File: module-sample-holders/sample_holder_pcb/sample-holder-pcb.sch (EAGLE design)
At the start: 12 parts, among them IC1 25AA040ST, IC2 DSPIC33CK256MP502-I_SS, Q1 PSMN013-30MLC, Q2 PSMN013-30MLC

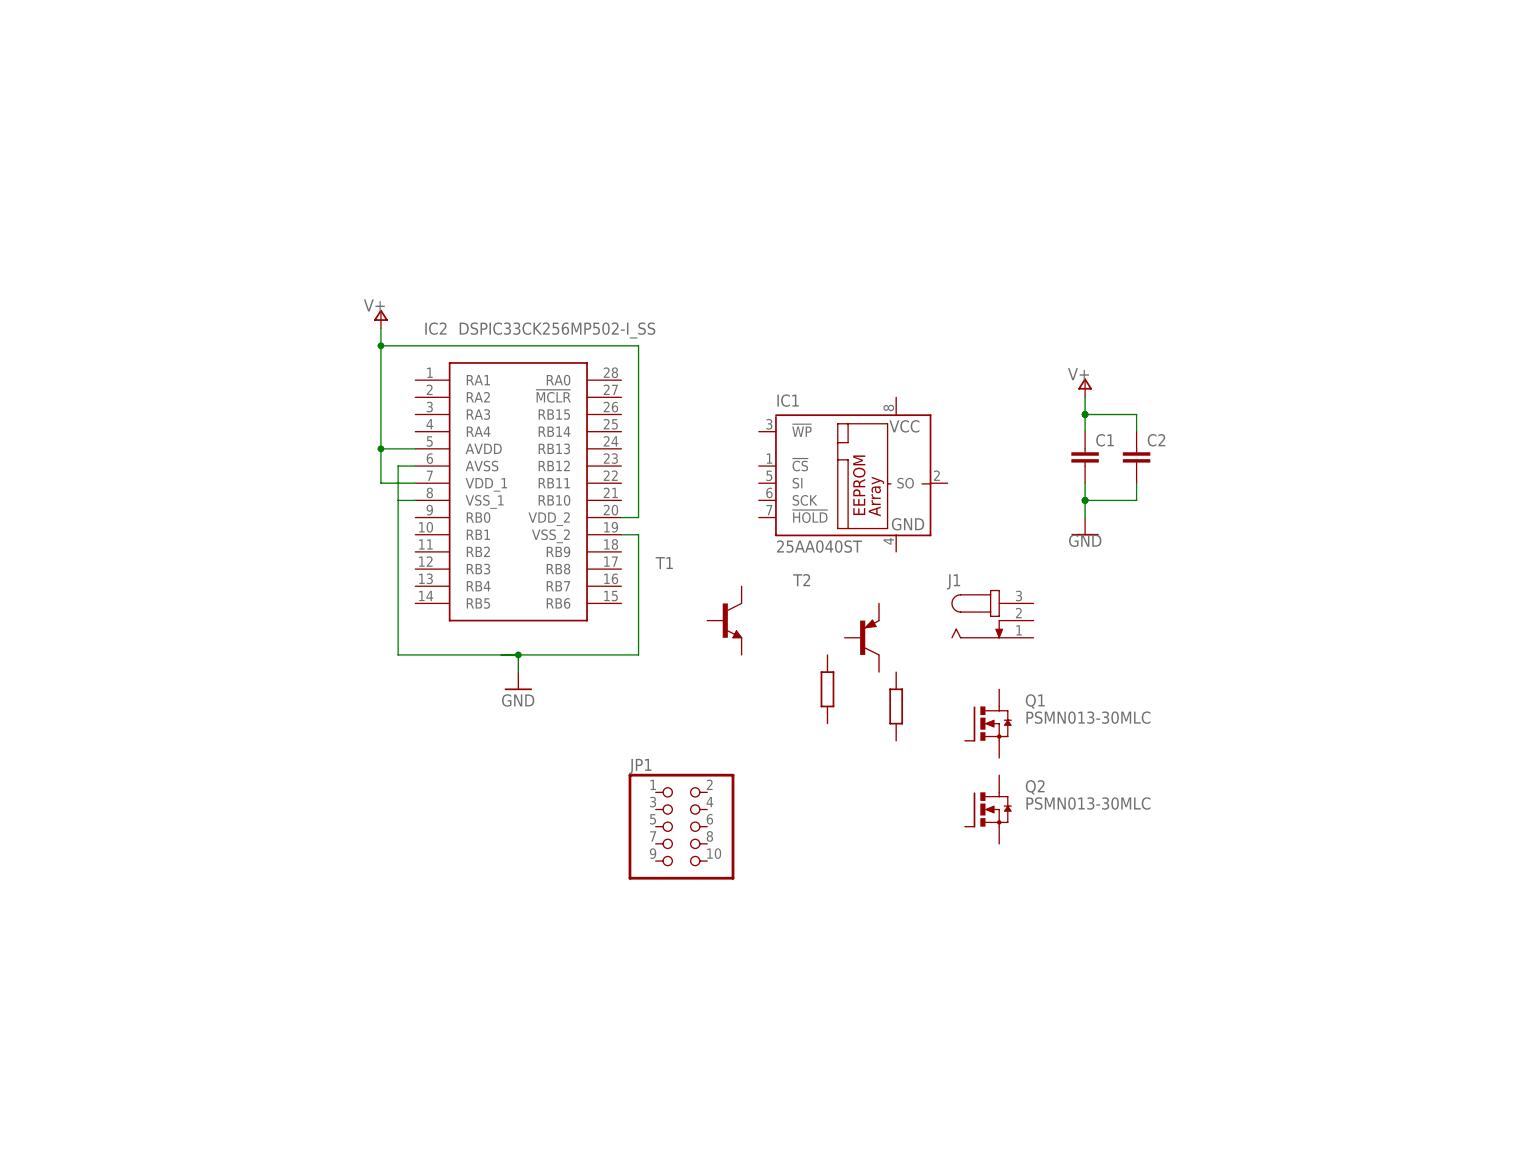
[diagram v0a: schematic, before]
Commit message: Submitting old PCB design before replacing with new design.
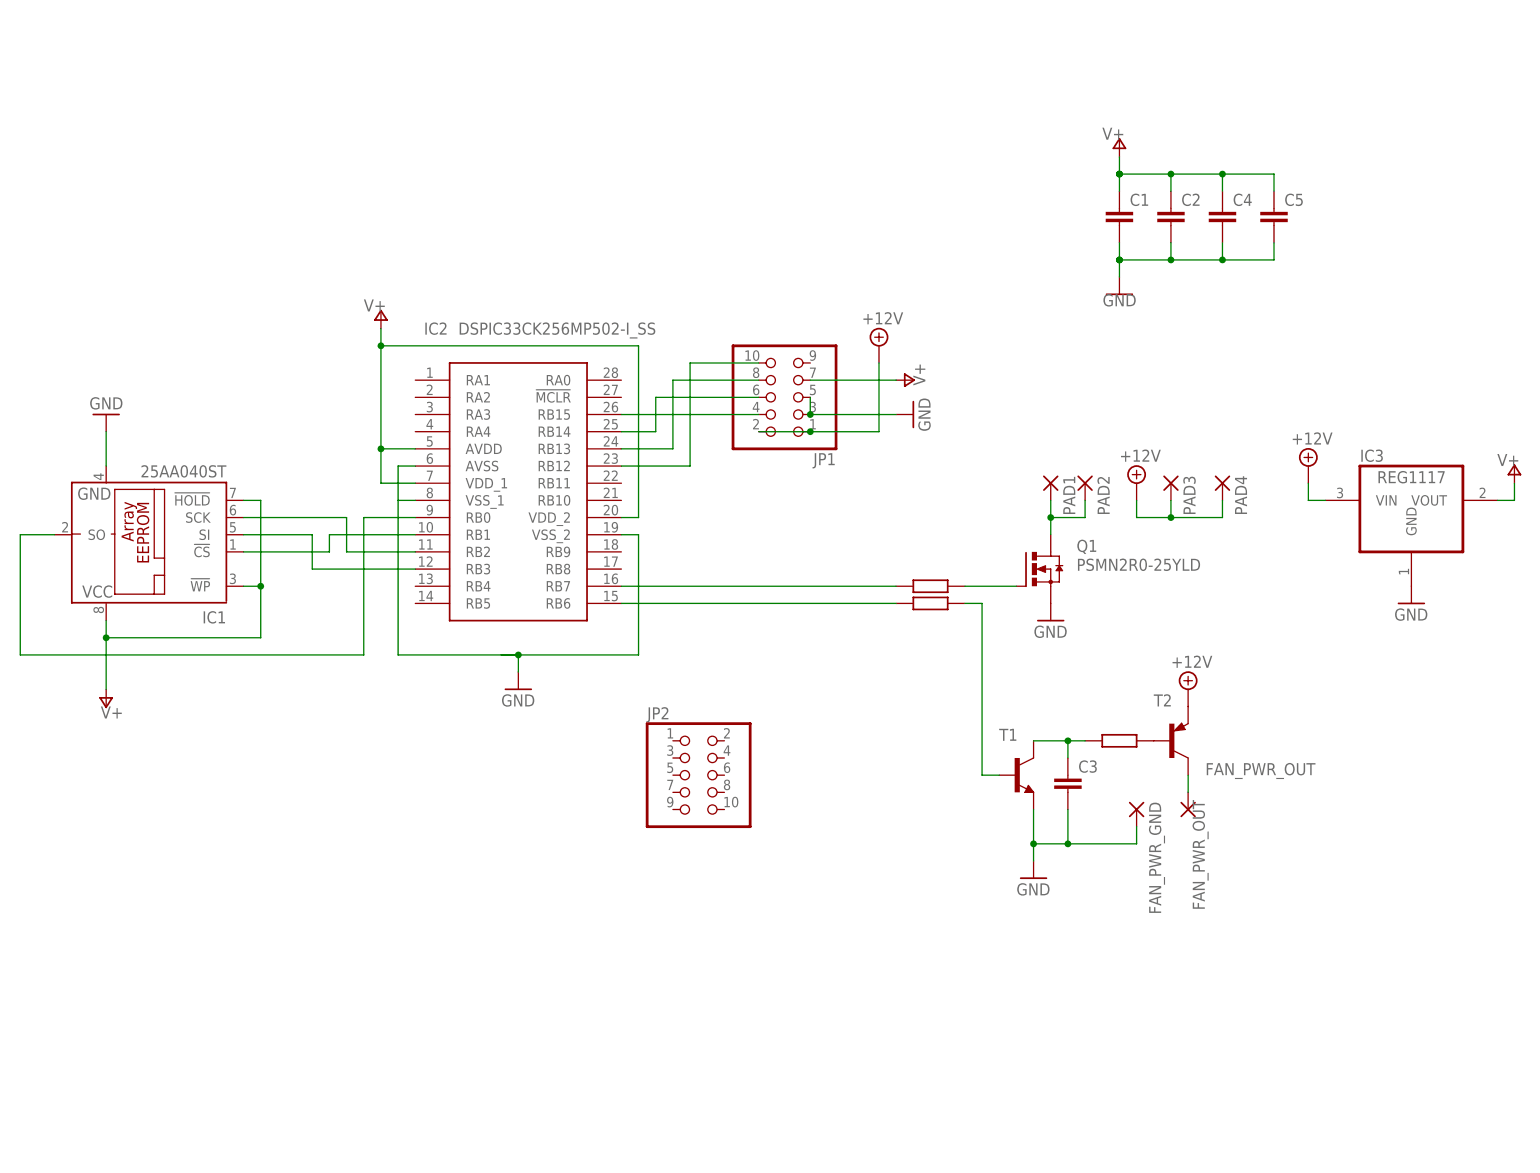
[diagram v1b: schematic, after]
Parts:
- removed J1: (no value), con-jack:JACK-PLUG1
- removed Q2: PSMN013-30MLC, transistor-power:PSMN013-30MLC
- added C3, C4, C5: (no value), rcl:C-EUC1206
- added FAN_PWR_GND, FAN_PWR_OUT: (no value), wirepad:1,6/0,8
- added IC3: REG1117, burr-brown:REG1117
- added JP2: (no value), pinhead:PINHD-2X5/90
- added PAD1, PAD2, PAD3, PAD4: (no value), wirepad:2,54/1,0
- added R3: (no value), rcl:R-EU_R1206
- Q1: MPN (none) -> PSMN2R0-25YLD
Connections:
- new net +12V: IC3.VIN, JP1.1, JP1.2, PAD3.P, PAD4.P, T2.E
- new net FAN_PWR_OUT: FAN_PWR_OUT.P, T2.C
- new net N$1: Q1.G, R2.1
- new net N$10: C3.1, R3.2, T1.C
- new net N$11: R3.1, T2.B
- new net N$12: IC2.RB12, JP1.10
- new net N$13: IC2.RB13, JP1.8
- new net N$14: IC2.RB14, JP1.6
- new net N$15: IC2.RB15, JP1.4
- new net N$16: IC2.RB6, R1.2
- new net N$17: IC2.RB7, R2.2
- new net N$2: IC1.SCK, IC2.RB2
- new net N$3: IC1.SO, IC2.RB0
- new net N$4: IC1.!CS, IC2.RB1
- new net N$5: IC1.SI, IC2.RB3
- new net N$8: PAD1.P, PAD2.P, Q1.D
- new net N$9: R1.1, T1.B
- net GND: now also C3.2, C4.2, C5.2, FAN_PWR_GND.P, IC1.GND, IC3.GND, JP1.3, JP1.5, Q1.S, T1.E
- net V+: now also C4.1, C5.1, IC1.!HOLD, IC1.!WP, IC1.VCC, IC3.VOUT, JP1.7
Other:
- moved on the sheet: C1, C2, IC1, JP1, Q1, T1, T2

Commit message: Sample Holder new design, first PCB submitted for manufacture.
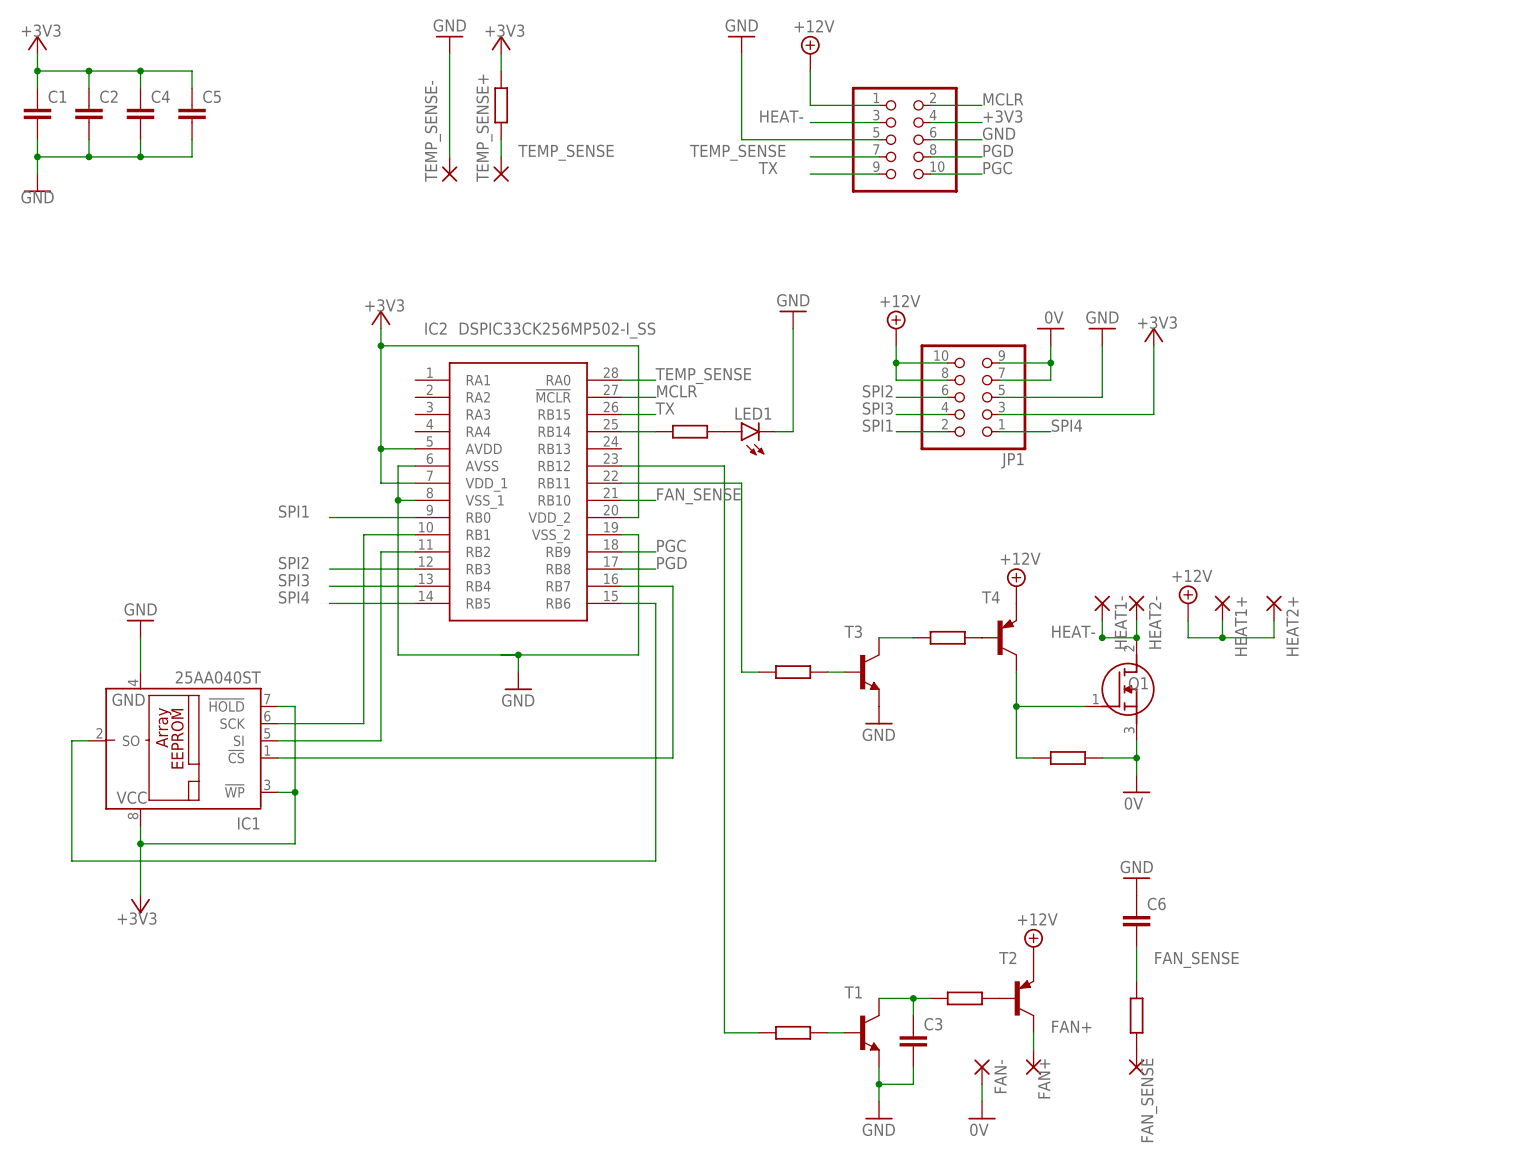
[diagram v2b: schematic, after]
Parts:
- removed FAN_PWR_GND, FAN_PWR_OUT: (no value), wirepad:1,6/0,8
- removed IC3: REG1117, burr-brown:REG1117
- removed PAD1, PAD2, PAD3, PAD4: (no value), wirepad:2,54/1,0
- added C6: (no value), rcl:C-EUC0603
- added FAN+, FAN-, FAN_SENSE, TEMP_SENSE+, TEMP_SENSE-: (no value), wirepad:1,6/0,8
- added HEAT1+, HEAT1-, HEAT2+, HEAT2-: (no value), wirepad:2,54/1,0
- added LED1: (no value), led:LEDSML0603
- added R4, R5, R6, R7, R8: (no value), rcl:R-EU_R0603
- added T3: (no value), transistor:MMBT3904LT1-NPN-SOT23-BEC
- added T4: (no value), transistor:MMBT3906LT1-PNP-SOT23-BEC
- C1, C2, C3, C4: device rcl:C-EUC1206 -> rcl:C-EUC0603
- Q1: value PSMN013-30MLC -> AUIRFU8403; device transistor-power:PSMN013-30MLC -> AUIRFU8403:AUIRFU8403; MPN PSMN2R0-25YLD -> (none)
- R1, R2, R3: device rcl:R-EU_R1206 -> rcl:R-EU_R0603
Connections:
- removed net FAN_PWR_OUT: FAN_PWR_OUT.P, T2.C
- removed net N$8: PAD1.P, PAD2.P, Q1.D
- removed net V+: C1.1, C2.1, C4.1, C5.1, IC1.!HOLD, IC1.!WP, IC1.VCC, IC2.AVDD, IC2.VDD_1, IC2.VDD_2, IC3.VOUT, JP1.7
- new net +3V3: C1.1, C2.1, C4.1, C5.1, IC1.!HOLD, IC1.!WP, IC1.VCC, IC2.AVDD, IC2.VDD_1, IC2.VDD_2, JP1.3, JP2.4, R7.1
- new net 0V: FAN-.P, JP1.7, JP1.9, Q1.S, R5.1
- new net FAN+: FAN+.P, T2.C
- new net FAN_SENSE: C6.2, IC2.RB10, R6.1
- new net HEAT-: HEAT1-.P, HEAT2-.P, JP2.3, Q1.D
- new net MCLR: IC2.!MCLR, JP2.2
- new net N$6: LED1.A, R8.2
- new net N$7: IC2.RB14, R8.1
- new net PGC: IC2.RB9, JP2.10
- new net PGD: IC2.RB8, JP2.8
- new net SPI1: IC2.RB0, JP1.2
- new net SPI2: IC2.RB3, JP1.6
- new net SPI3: IC2.RB4, JP1.4
- new net SPI4: IC2.RB5, JP1.1
- new net TEMP_SENSE: IC2.RA0, JP2.7, R7.2, TEMP_SENSE+.P
- new net TX: IC2.RB15, JP2.9
- net +12V: now also HEAT1+.P, HEAT2+.P, JP1.10, JP1.8, JP2.1, T4.E; no longer IC3.VIN, JP1.1, JP1.2, PAD3.P, PAD4.P
- net GND: now also C6.1, JP2.5, JP2.6, LED1.C, T3.E, TEMP_SENSE-.P; no longer FAN_PWR_GND.P, IC3.GND, JP1.3, Q1.S
- net N$1: now also T3.B; no longer Q1.G
- net N$12: now also IC2.RB11, R2.2; no longer IC2.RB12, JP1.10
- net N$13: now also IC1.SI, IC2.RB2; no longer IC2.RB13, JP1.8
- net N$14: now also IC1.SCK, IC2.RB1; no longer IC2.RB14, JP1.6
- net N$15: now also IC1.SO, IC2.RB6; no longer IC2.RB15, JP1.4
- net N$16: now also IC1.!CS, IC2.RB7; no longer IC2.RB6, R1.2
- net N$17: now also IC2.RB12, R1.2; no longer IC2.RB7, R2.2
- net N$2: now also R4.2, T3.C; no longer IC1.SCK, IC2.RB2
- net N$3: now also R4.1, T4.B; no longer IC1.SO, IC2.RB0
- net N$4: now also Q1.G, R5.2, T4.C; no longer IC1.!CS, IC2.RB1
- net N$5: now also FAN_SENSE.P, R6.2; no longer IC1.SI, IC2.RB3
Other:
- moved on the sheet: C1, C2, C3, C4, C5, IC1, JP1, T1, T2

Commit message: Minor changes to PCB: 1mm larger, MCLR resistor + cap added, thicker trace to external heater.  Second manufacturing, not express.
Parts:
- added C7: (no value), rcl:C-EUC0603
- added R9: 10k, rcl:R-EU_R0603
- C1, C2, C4, C6: value (none) -> 100nf
- C3: value (none) -> 1nf
- C5: value (none) -> 10uf
- R1, R2, R3, R4, R5, R6: value (none) -> 1k
- R7: value (none) -> 3.3k
- R8: value (none) -> 120
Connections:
- net +3V3: now also R9.1
- net GND: now also C7.1
- net MCLR: now also C7.2, R9.2

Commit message: Changed fan sense resistor from 1k to 510, because at low speed the fan feedback would not pull low enough.
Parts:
- R6: value 1k -> 510R
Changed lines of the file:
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@@
 <?xml version="1.0" encoding="utf-8"?>
 <!DOCTYPE eagle SYSTEM "eagle.dtd">
-<eagle version="9.5.2">
+<eagle version="9.5.1">
 <drawing>
 <settings>
@@
 <part name="GND10" library="supply1" library_urn="urn:adsk.eagle:library:371" deviceset="0V" device=""/>
 <part name="FAN_SENSE" library="wirepad" library_urn="urn:adsk.eagle:library:412" deviceset="1,6/0,8" device="" package3d_urn="urn:adsk.eagle:package:30830/1"/>
-<part name="R6" library="rcl" library_urn="urn:adsk.eagle:library:334" deviceset="R-EU_" device="R0603" package3d_urn="urn:adsk.eagle:package:23555/3" value="1k"/>
+<part name="R6" library="rcl" library_urn="urn:adsk.eagle:library:334" deviceset="R-EU_" device="R0603" package3d_urn="urn:adsk.eagle:package:23555/3" value="510R"/>
 <part name="C6" library="rcl" library_urn="urn:adsk.eagle:library:334" deviceset="C-EU" device="C0603" package3d_urn="urn:adsk.eagle:package:23616/2" value="100nf"/>
 <part name="GND11" library="supply1" library_urn="urn:adsk.eagle:library:371" deviceset="GND" device=""/>

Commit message: Added SPI names.
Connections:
- net SPI1 renamed SPI_SS
- net SPI2 renamed SPI_MISO
- net SPI3 renamed SPI_MOSI
- net SPI4 renamed SPI_CLK
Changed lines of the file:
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@@
 </segment>
 </net>
-<net name="SPI1" class="0">
+<net name="SPI_SS" class="0">
 <segment>
 <pinref part="IC2" gate="G$1" pin="RB0"/>
@@
 </segment>
 </net>
-<net name="SPI2" class="0">
+<net name="SPI_MISO" class="0">
 <segment>
 <pinref part="IC2" gate="G$1" pin="RB3"/>
@@
 </segment>
 </net>
-<net name="SPI3" class="0">
+<net name="SPI_MOSI" class="0">
 <segment>
 <pinref part="IC2" gate="G$1" pin="RB4"/>
@@
 </segment>
 </net>
-<net name="SPI4" class="0">
+<net name="SPI_CLK" class="0">
 <segment>
 <pinref part="IC2" gate="G$1" pin="RB5"/>

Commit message: PCB documentation.
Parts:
- C7: value (none) -> Unfitted
- T1, T3: value (none) -> NPN
- T2, T4: value (none) -> PNP
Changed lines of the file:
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@@
 <?xml version="1.0" encoding="utf-8"?>
 <!DOCTYPE eagle SYSTEM "eagle.dtd">
-<eagle version="9.5.1">
+<eagle version="9.5.2">
 <drawing>
 <settings>
@@
 <part name="JP1" library="pinhead" library_urn="urn:adsk.eagle:library:325" deviceset="PINHD-2X5" device="/90" package3d_urn="urn:adsk.eagle:package:22471/2"/>
 <part name="IC1" library="microchip" library_urn="urn:adsk.eagle:library:294" deviceset="25*" device="ST" package3d_urn="urn:adsk.eagle:package:20813/2" technology="AA040"/>
-<part name="T1" library="transistor" library_urn="urn:adsk.eagle:library:402" deviceset="*-NPN-" device="SOT23-BEC" package3d_urn="urn:adsk.eagle:package:28748/2" technology="MMBT3904LT1"/>
-<part name="T2" library="transistor" library_urn="urn:adsk.eagle:library:402" deviceset="*-PNP-" device="SOT23-BEC" package3d_urn="urn:adsk.eagle:package:28748/2" technology="MMBT3906LT1"/>
+<part name="T1" library="transistor" library_urn="urn:adsk.eagle:library:402" deviceset="*-NPN-" device="SOT23-BEC" package3d_urn="urn:adsk.eagle:package:28748/2" technology="MMBT3904LT1" value="NPN"/>
+<part name="T2" library="transistor" library_urn="urn:adsk.eagle:library:402" deviceset="*-PNP-" device="SOT23-BEC" package3d_urn="urn:adsk.eagle:package:28748/2" technology="MMBT3906LT1" value="PNP"/>
 <part name="Q1" library="AUIRFU8403" deviceset="AUIRFU8403" device=""/>
 <part name="SUPPLY1" library="supply2" library_urn="urn:adsk.eagle:library:372" deviceset="+12V" device=""/>
@@
 <part name="JP2" library="pinhead" library_urn="urn:adsk.eagle:library:325" deviceset="PINHD-2X5" device="/90" package3d_urn="urn:adsk.eagle:package:22471/2"/>
 <part name="P+5" library="supply1" library_urn="urn:adsk.eagle:library:371" deviceset="+3V3" device=""/>
-<part name="T3" library="transistor" library_urn="urn:adsk.eagle:library:402" deviceset="*-NPN-" device="SOT23-BEC" package3d_urn="urn:adsk.eagle:package:28748/2" technology="MMBT3904LT1"/>
+<part name="T3" library="transistor" library_urn="urn:adsk.eagle:library:402" deviceset="*-NPN-" device="SOT23-BEC" package3d_urn="urn:adsk.eagle:package:28748/2" technology="MMBT3904LT1" value="NPN"/>
 <part name="R4" library="rcl" library_urn="urn:adsk.eagle:library:334" deviceset="R-EU_" device="R0603" package3d_urn="urn:adsk.eagle:package:23555/3" value="1k"/>
-<part name="T4" library="transistor" library_urn="urn:adsk.eagle:library:402" deviceset="*-PNP-" device="SOT23-BEC" package3d_urn="urn:adsk.eagle:package:28748/2" technology="MMBT3906LT1"/>
+<part name="T4" library="transistor" library_urn="urn:adsk.eagle:library:402" deviceset="*-PNP-" device="SOT23-BEC" package3d_urn="urn:adsk.eagle:package:28748/2" technology="MMBT3906LT1" value="PNP"/>
 <part name="R5" library="rcl" library_urn="urn:adsk.eagle:library:334" deviceset="R-EU_" device="R0603" package3d_urn="urn:adsk.eagle:package:23555/3" value="1k"/>
 <part name="SUPPLY5" library="supply2" library_urn="urn:adsk.eagle:library:372" deviceset="+12V" device=""/>
@@
 <part name="R8" library="rcl" library_urn="urn:adsk.eagle:library:334" deviceset="R-EU_" device="R0603" package3d_urn="urn:adsk.eagle:package:23555/3" value="120"/>
 <part name="R9" library="rcl" library_urn="urn:adsk.eagle:library:334" deviceset="R-EU_" device="R0603" package3d_urn="urn:adsk.eagle:package:23555/3" value="10k"/>
-<part name="C7" library="rcl" library_urn="urn:adsk.eagle:library:334" deviceset="C-EU" device="C0603" package3d_urn="urn:adsk.eagle:package:23616/2"/>
+<part name="C7" library="rcl" library_urn="urn:adsk.eagle:library:334" deviceset="C-EU" device="C0603" package3d_urn="urn:adsk.eagle:package:23616/2" value="Unfitted"/>
 </parts>
 <sheets>
